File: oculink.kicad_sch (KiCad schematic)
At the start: 25 parts, among them J2 OCuLink_x4_Amphenol_G14A42121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, U5 ESD204DQAR, U7 ESD204DQAR, U8 ESD204DQAR, U9 ESD204DQAR

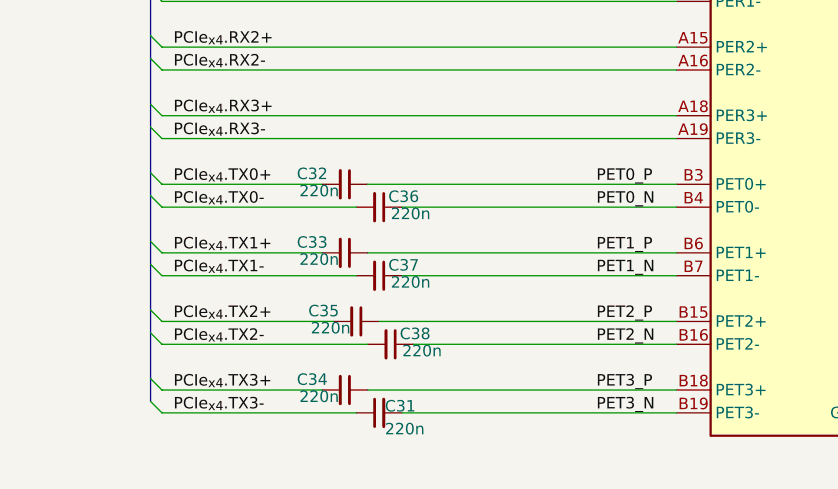
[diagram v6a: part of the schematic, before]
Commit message: [#57056] Add PCIe redriver for OCuLink
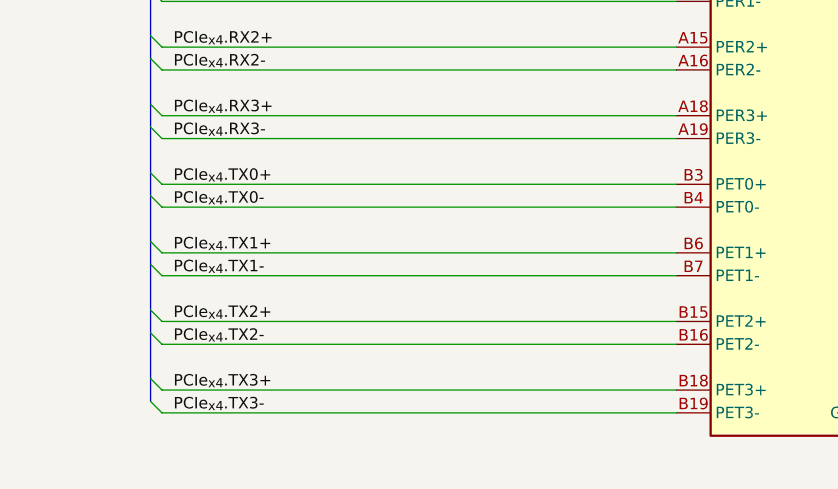
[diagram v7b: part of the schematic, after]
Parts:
- removed C31, C32, C33, C34, C35, C36, C37, C38: C_220n_0402, antmicro-footprints:C_0402_1005Metric, symbol antmicroCapacitors0402:C_220n_0402
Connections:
- net PCIe_{x4}.TX0+: now also J2.B3 (PET0+)
- net PCIe_{x4}.TX0-: now also J2.B4 (PET0-)
- net PCIe_{x4}.TX1+: now also J2.B6 (PET1+)
- net PCIe_{x4}.TX1-: now also J2.B7 (PET1-)
- net PCIe_{x4}.TX2+: now also J2.B15 (PET2+)
- net PCIe_{x4}.TX2-: now also J2.B16 (PET2-)
- net PCIe_{x4}.TX3+: now also J2.B18 (PET3+)
- net PCIe_{x4}.TX3-: now also J2.B19 (PET3-)
- net PET0_N: no longer J2.B4 (PET0-)
- net PET0_P: no longer J2.B3 (PET0+)
- net PET1_N: no longer J2.B7 (PET1-)
- net PET1_P: no longer J2.B6 (PET1+)
- net PET2_N: no longer J2.B16 (PET2-)
- net PET2_P: no longer J2.B15 (PET2+)
- net PET3_N: no longer J2.B19 (PET3-)
- net PET3_P: no longer J2.B18 (PET3+)

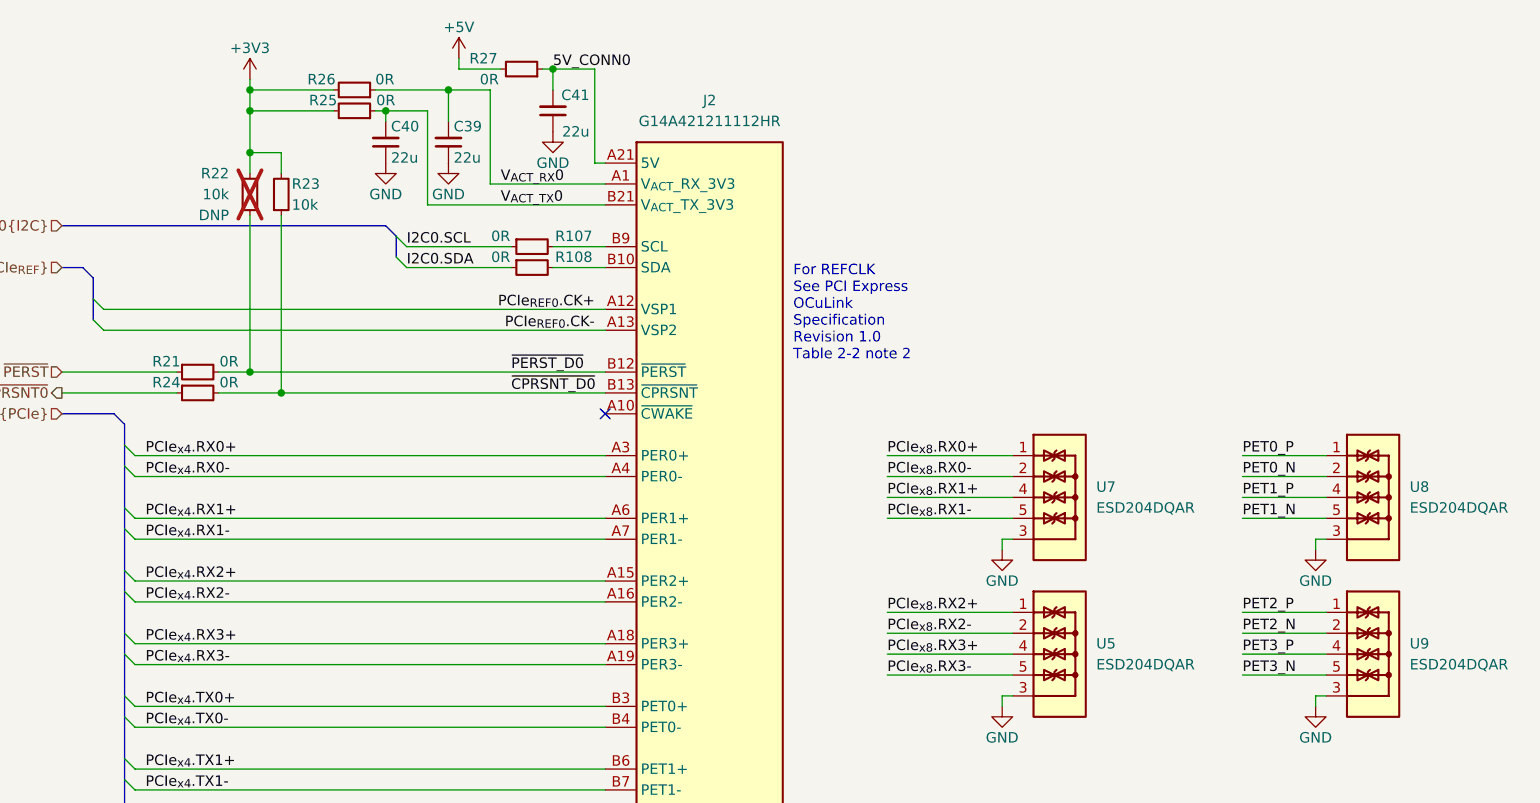
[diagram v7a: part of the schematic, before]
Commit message: [#58137] Update backplane connector pinout
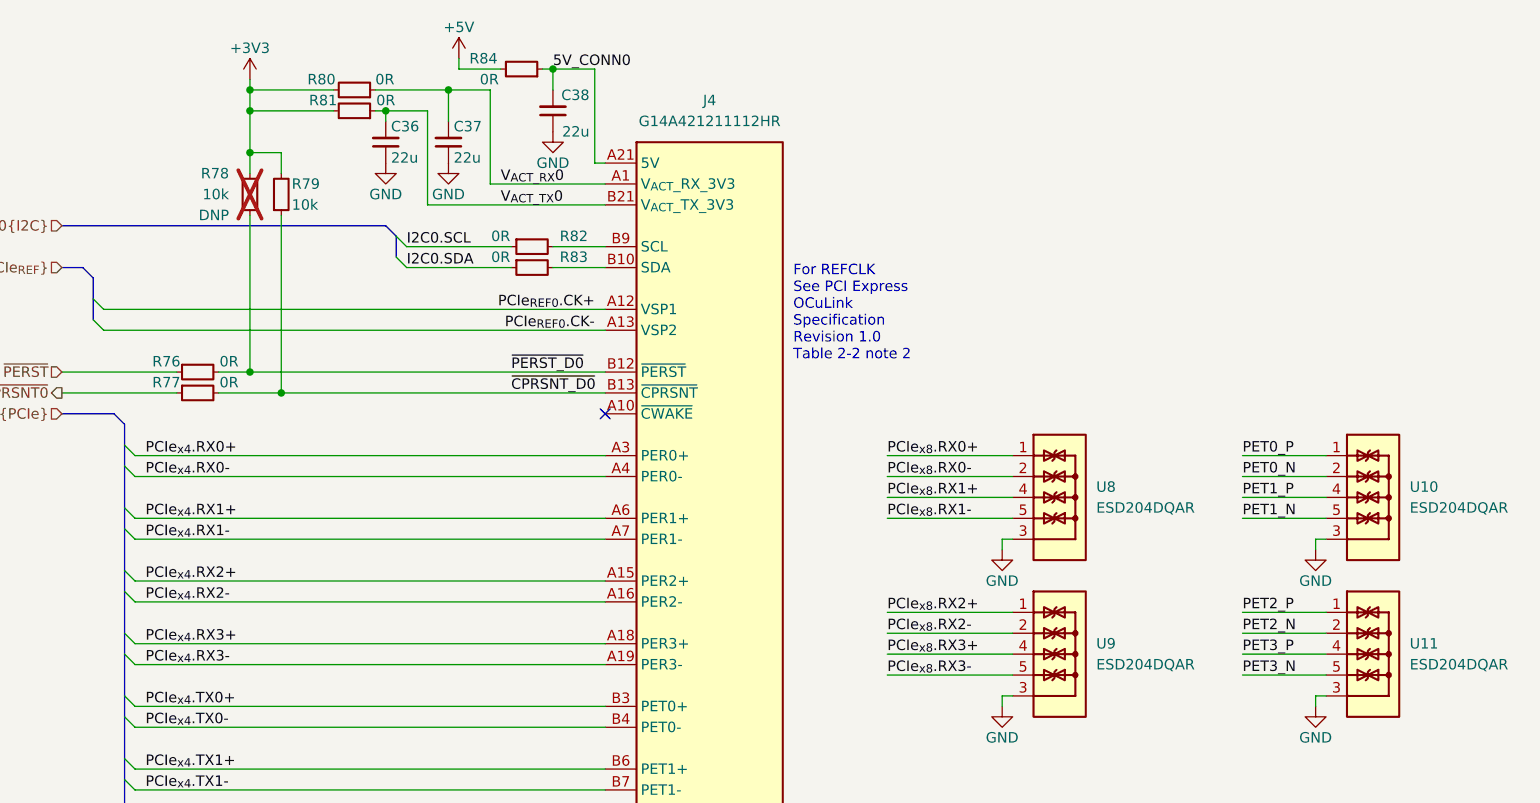
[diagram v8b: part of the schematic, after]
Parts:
- renumbered C40 to C36, C39 to C37, C41 to C38, J2 to J4, R21 to R76, R24 to R77, R22 to R78, R23 to R79, R26 to R80, R25 to R81, R107 to R82, R108 to R83, R27 to R84, U8 to U10, U9 to U11, U7 to U8, U5 to U9
